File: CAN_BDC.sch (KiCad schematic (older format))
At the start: 35 parts, among them P1 CONN_01X02, P2 CONN_01X05, P3 CONN_01X02, P4 CONN_01X02, P5 CONN_01X02, P6 CONN_01X02, P7 CONN_01X04, P8 CONN_01X01, P9 CONN_01X02, U1 PSD2CAN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

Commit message: Footprint update.
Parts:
- L2: footprint Resistors_SMD:R_0805 -> Capacitors_SMD:C_1206
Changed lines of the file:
@@
 F 0 "L2" H 9500 5900 50  0000 C CNN
 F 1 "1uH" H 9500 5650 50  0000 C CNN
-F 2 "Resistors_SMD:R_0805" H 9500 5750 50  0001 C CNN
+F 2 "Capacitors_SMD:C_1206" H 9500 5750 50  0001 C CNN
 F 3 "" H 9500 5750 50  0000 C CNN
 	1    9500 5750

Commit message: Root full
Root full
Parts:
- L1: footprint usb_ccb_custom:DE0704_Coil -> usb_ccb_custom:DE0704_Coil_2
- P2: footprint usb_ccb_custom:swd_smd_conn5 -> usb_ccb_custom:swd_smd_conn5_x2
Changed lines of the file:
@@
 F 0 "P2" H 1319 1461 50  0000 C CNN
 F 1 "CONN_01X05" H 1319 1460 50  0001 C CNN
-F 2 "usb_ccb_custom:swd_smd_conn5" H 1319 1461 50  0001 C CNN
+F 2 "usb_ccb_custom:swd_smd_conn5_x2" H 1319 1461 50  0001 C CNN
 F 3 "" H 1400 1800 50  0000 C CNN
 	1    1400 1800
@@
 	-1   0    0    1
 $EndComp
+Text GLabel 3450 1500 0    60   Input ~ 0
+DRV_nENABLE
+Text GLabel 3450 1400 0    60   Input ~ 0
+DRV_MS1
+Text GLabel 5100 1400 2    60   Input ~ 0
+DRV_MS2
+Text GLabel 5100 1500 2    60   Input ~ 0
+DRV_MS3
+Text GLabel 5100 1600 2    60   Input ~ 0
+DRV_nRESET
+Text GLabel 5100 1700 2    60   Input ~ 0
+DRV_nSLEEP
+Text GLabel 5100 1800 2    60   Input ~ 0
+DRV_STEP
 Text GLabel 5100 1900 2    60   Input ~ 0
-DRV_nENABLE
-Text GLabel 5100 1800 2    60   Input ~ 0
-DRV_MS1
-Text GLabel 5100 1700 2    60   Input ~ 0
-DRV_MS2
-Text GLabel 5100 1600 2    60   Input ~ 0
-DRV_MS3
-Text GLabel 5100 1500 2    60   Input ~ 0
-DRV_nRESET
-Text GLabel 5100 1400 2    60   Input ~ 0
-DRV_nSLEEP
-Text GLabel 3450 1400 0    60   Input ~ 0
-DRV_STEP
-Text GLabel 3450 1500 0    60   Input ~ 0
 DRV_DIR
 $Comp
@@
 F 0 "L1" V 7000 5000 50  0000 L CNN
 F 1 "220uH" V 6850 4850 50  0000 L CNN
-F 2 "usb_ccb_custom:DE0704_Coil" H 6900 5050 50  0001 C CNN
+F 2 "usb_ccb_custom:DE0704_Coil_2" H 6900 5050 50  0001 C CNN
 F 3 "" H 6900 5050 50  0000 C CNN
 	1    6900 5050

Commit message: Gerber generation
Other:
- note added: "consider TCAN332DR"
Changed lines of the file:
@@
 Wire Notes Line
 	1800 3250 1800 2200
+Text Notes 2800 5750 0    60   ~ 0
+consider  TCAN332DR
 $EndSCHEMATC

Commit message: Buck-converter update.
Buck-converter update.
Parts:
- removed C5: 470p, Capacitors_SMD:C_0805, symbol CP1
- removed C6: 330u, Capacitors_SMD:c_elec_6.3x7.7, symbol CP1
- removed D1: 1N5819, Resistors_SMD:R_1206, symbol D_Schottky
- removed L1: 220uH, usb_ccb_custom:DE0704_Coil_2, symbol L_Small
- removed P8: CONN_01X01, usb_ccb_custom:smd1Conn, symbol CONN_01X01
- removed R1: 2,2k, Resistors_SMD:R_0603, symbol R
- removed R2: 0.33, Resistors_SMD:R_0603, symbol R
- removed R3: 3,9k, Resistors_SMD:R_0603, symbol R
- removed R6: 0, Resistors_SMD:R_0603, symbol R
- removed U5: MC33063, usb_ccb_custom:SOIC-8, symbol MC33063
- added U5: Mini-360, usb_ccb_custom:Mini-360, symbol Mini-360
- P2: footprint usb_ccb_custom:swd_smd_conn5_x2 -> usb_ccb_custom:swd_smd_conn5
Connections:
- wire segments 70 -> 48
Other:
- note added: "NRST\nGND\nSWCLK\nSWDIO\nVTRG"
- note removed: "GND\nSWDIO\nSWCLK\nNRST\nVTRG"
- moved on the sheet: C4, C7, L2, P6

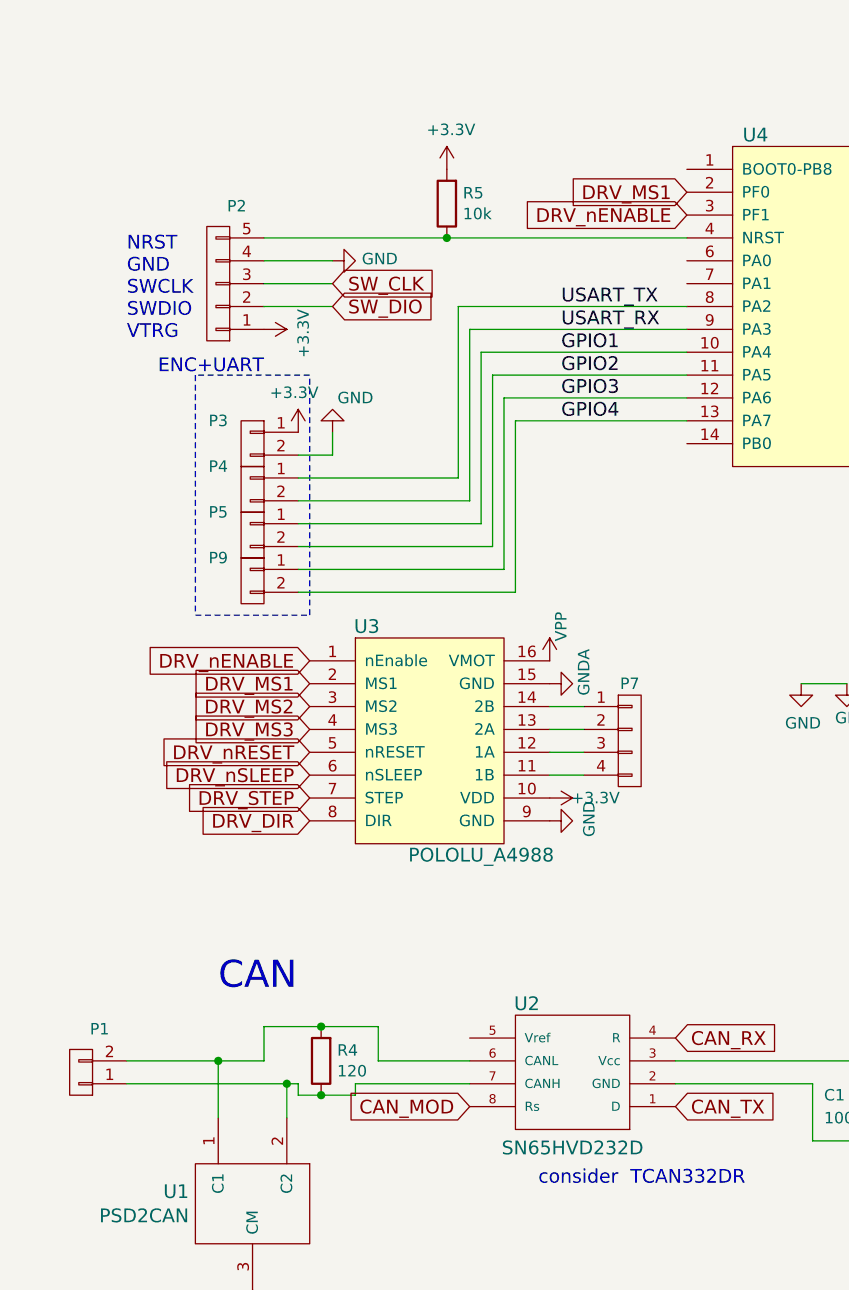
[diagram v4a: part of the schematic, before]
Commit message: Connector Footprint update
Connector Footprint update
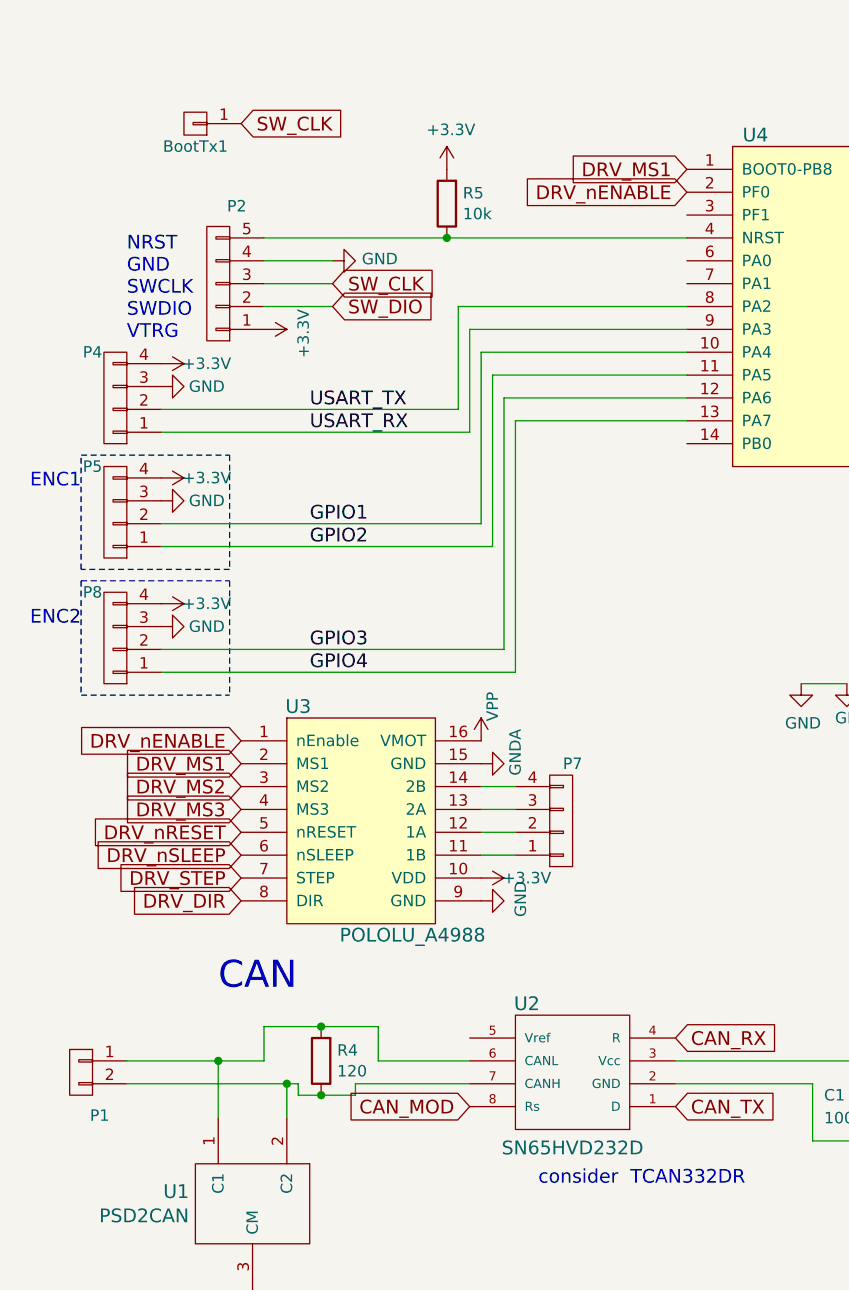
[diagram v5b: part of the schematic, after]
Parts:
- removed P3, P4, P5, P9: CONN_01X02, Pin_Headers:Pin_Header_Straight_1x02_Pitch2.00mm, symbol CONN_01X02
- added BootTx1: CONN_01X01, usb_ccb_custom:1pin, symbol CONN_01X01
- added P4, P5, P8: CONN_01X04, Pin_Headers:Pin_Header_Angled_1x04_Pitch2.54mm, symbol CONN_01X04
- C4: footprint Capacitors_SMD:c_elec_6.3x7.7 -> Capacitors_SMD:c_elec_6.3x5.3
- P1: footprint Pin_Headers:Pin_Header_Straight_1x02_Pitch2.00mm -> Pin_Headers:Pin_Header_Angled_1x02_Pitch2.54mm
- P6: footprint Pin_Headers:Pin_Header_Straight_1x02_Pitch2.00mm -> Terminal_Blocks:TerminalBlock_Pheonix_MPT-2.54mm_2pol
- P7: footprint Pin_Headers:Pin_Header_Straight_1x04 -> Terminal_Blocks:TerminalBlock_Pheonix_MPT-2.54mm_4pol
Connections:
- net +3V3: now also P4.4 (P4), P5.4 (P4), P8.4 (P4)
- net DRV_MS1: now also U4.1 (BOOT0-PB8); no longer U4.2 (PF0)
- net DRV_nENABLE: now also U4.2 (PF0); no longer U4.3 (PF1)
- net GND: now also P4.3 (P3), P5.3 (P3), P8.3 (P3)
- net GPIO1: now also P5.2 (P2)
- net GPIO2: now also P5.1 (P1)
- net GPIO3: now also P8.2 (P2)
- net GPIO4: now also P8.1 (P1)
- net SW_CLK: now also BootTx1.1 (P1)
- net USART_RX: now also P4.1 (P1)
- net USART_TX: now also P4.2 (P2)
- net at R4.2, U1.1 (C1), U2.6 (CANL): now also P1.1 (P1); no longer P1.2 (P2)
- net at R4.1, U1.2 (C2), U2.7 (CANH): now also P1.2 (P2); no longer P1.1 (P1)
- net at P7.1 (P1): now also U3.11 (1B); no longer U3.14 (2B)
- net at P7.2 (P2): now also U3.12 (1A); no longer U3.13 (2A)
- net at P7.3 (P3): now also U3.13 (2A); no longer U3.12 (1A)
- net at P7.4 (P4): now also U3.14 (2B); no longer U3.11 (1B)
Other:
- note added: "ENC1"
- note added: "ENC2"
- note removed: "ENC+UART"
- moved on the sheet: P7, U3

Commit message: Layout update
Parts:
- removed BootTx1: CONN_01X01, usb_ccb_custom:1pin, symbol CONN_01X01
- added P3, P9: CONN_01X02, Pin_Headers:Pin_Header_Straight_1x02_Pitch2.54mm, symbol CONN_01X02
- P1: footprint Pin_Headers:Pin_Header_Angled_1x02_Pitch2.54mm -> Pin_Headers:Pin_Header_Straight_1x02_Pitch2.54mm
- P4, P5, P8: footprint Pin_Headers:Pin_Header_Angled_1x04_Pitch2.54mm -> Pin_Headers:Pin_Header_Straight_1x04_Pitch2.54mm
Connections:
- net DRV_DIR: now also P3.1 (P1)
- net DRV_MS1: now also U4.2 (PF0); no longer U4.1 (BOOT0-PB8)
- net DRV_nENABLE: now also U4.3 (PF1); no longer U4.2 (PF0)
- net GND: now also P6.1 (P1); no longer P6.2 (P2)
- net SW_CLK: now also P3.2 (P2)
- net VPP: now also P6.2 (P2); no longer P6.1 (P1)
- net at P1.1 (P1), R4.2, U1.1 (C1)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: now also P9.1 (P1)
- net at P1.2 (P2), R4.1, U1.2 (C2)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: now also P9.2 (P2)

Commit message: layout update
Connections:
- net GPIO1: now also P8.1 (P1), U4.6 (PA0); no longer P5.2 (P2), U4.10 (PA4)
- net GPIO2: now also P8.2 (P2), U4.7 (PA1); no longer P5.1 (P1), U4.11 (PA5)
- net GPIO3: now also P5.1 (P1); no longer P8.2 (P2)
- net GPIO4: now also P5.2 (P2); no longer P8.1 (P1)
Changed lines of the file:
@@
 $EndDescr
 $Comp
-L GND #PWR18
+L GND #PWR01
 U 1 1 570561B2
 P 4250 2800
-F 0 "#PWR18" H 4250 2550 50  0001 C CNN
+F 0 "#PWR01" H 4250 2550 50  0001 C CNN
 F 1 "GND" H 4258 2627 50  0000 C CNN
 F 2 "" H 4250 2800 50  0000 C CNN
@@
 NRST\nGND\nSWCLK\nSWDIO\nVTRG
 $Comp
-L +3.3V #PWR10
+L +3.3V #PWR02
 U 1 1 5706E500
 P 2400 1300
-F 0 "#PWR10" H 2400 1150 50  0001 C CNN
+F 0 "#PWR02" H 2400 1150 50  0001 C CNN
 F 1 "+3.3V" H 2418 1473 50  0000 C CNN
 F 2 "" H 2400 1300 50  0000 C CNN
@@
 $EndComp
 $Comp
-L +3.3V #PWR17
+L +3.3V #PWR03
 U 1 1 5706E57B
 P 4250 1000
-F 0 "#PWR17" H 4250 850 50  0001 C CNN
+F 0 "#PWR03" H 4250 850 50  0001 C CNN
 F 1 "+3.3V" H 4268 1173 50  0000 C CNN
 F 2 "" H 4250 1000 50  0000 C CNN
@@
 $EndComp
 $Comp
-L GND #PWR22
+L GND #PWR04
 U 1 1 5706EDB2
 P 5200 3100
-F 0 "#PWR22" H 5200 2850 50  0001 C CNN
+F 0 "#PWR04" H 5200 2850 50  0001 C CNN
 F 1 "GND" H 5208 2927 50  0000 C CNN
 F 2 "" H 5200 3100 50  0000 C CNN
@@
 $EndComp
 $Comp
-L GND #PWR24
+L GND #PWR05
 U 1 1 5706EDDA
 P 5600 3100
-F 0 "#PWR24" H 5600 2850 50  0001 C CNN
+F 0 "#PWR05" H 5600 2850 50  0001 C CNN
 F 1 "GND" H 5608 2927 50  0000 C CNN
 F 2 "" H 5600 3100 50  0000 C CNN
@@
 $EndComp
 $Comp
-L +3.3V #PWR23
+L +3.3V #PWR06
 U 1 1 5706EE52
 P 5600 2800
-F 0 "#PWR23" H 5600 2650 50  0001 C CNN
+F 0 "#PWR06" H 5600 2650 50  0001 C CNN
 F 1 "+3.3V" H 5618 2973 50  0000 C CNN
 F 2 "" H 5600 2800 50  0000 C CNN
@@
 $EndComp
 $Comp
-L +3.3V #PWR21
+L +3.3V #PWR07
 U 1 1 5706EEDE
 P 5200 2800
-F 0 "#PWR21" H 5200 2650 50  0001 C CNN
+F 0 "#PWR07" H 5200 2650 50  0001 C CNN
 F 1 "+3.3V" H 5218 2973 50  0000 C CNN
 F 2 "" H 5200 2800 50  0000 C CNN
@@
 $EndComp
 $Comp
-L +3.3V #PWR20
+L +3.3V #PWR08
 U 1 1 5708A6C5
 P 4550 5200
-F 0 "#PWR20" H 4550 5050 50  0001 C CNN
+F 0 "#PWR08" H 4550 5050 50  0001 C CNN
 F 1 "+3.3V" H 4568 5373 50  0000 C CNN
 F 2 "" H 4550 5200 50  0000 C CNN
@@
 $EndComp
 $Comp
-L GND #PWR19
+L GND #PWR09
 U 1 1 5708A9FB
 P 4250 5550
-F 0 "#PWR19" H 4250 5300 50  0001 C CNN
+F 0 "#PWR09" H 4250 5300 50  0001 C CNN
 F 1 "GND" V 4258 5422 50  0000 R CNN
 F 2 "" H 4250 5550 50  0000 C CNN
@@
 $EndComp
 $Comp
-L GND #PWR7
+L GND #PWR010
 U 1 1 5708D67B
 P 1550 6200
-F 0 "#PWR7" H 1550 5950 50  0001 C CNN
+F 0 "#PWR010" H 1550 5950 50  0001 C CNN
 F 1 "GND" V 1558 6072 50  0000 R CNN
 F 2 "" H 1550 6200 50  0000 C CNN
@@
 SW_DIO
 $Comp
-L +3.3V #PWR8
+L +3.3V #PWR011
 U 1 1 57800AA2
 P 1600 2000
-F 0 "#PWR8" H 1600 1850 50  0001 C CNN
+F 0 "#PWR011" H 1600 1850 50  0001 C CNN
 F 1 "+3.3V" H 1618 2173 50  0000 C CNN
 F 2 "" H 1600 2000 50  0000 C CNN
@@
 $EndComp
 $Comp
-L +3.3V #PWR32
+L +3.3V #PWR012
 U 1 1 57F96BE3
 P 9000 2100
-F 0 "#PWR32" H 9000 1950 50  0001 C CNN
+F 0 "#PWR012" H 9000 1950 50  0001 C CNN
 F 1 "+3.3V" H 9100 2250 50  0000 C CNN
 F 2 "" H 9000 2100 50  0000 C CNN
@@
 $EndComp
 $Comp
-L GND #PWR9
+L GND #PWR013
 U 1 1 57056C83
 P 1900 1700
-F 0 "#PWR9" H 1900 1450 50  0001 C CNN
+F 0 "#PWR013" H 1900 1450 50  0001 C CNN
 F 1 "GND" V 1908 1572 50  0000 R CNN
 F 2 "" H 1900 1700 50  0000 C CNN
@@
 $EndComp
 $Comp
-L VPP #PWR29
+L VPP #PWR014
 U 1 1 5802A676
 P 7850 1550
-F 0 "#PWR29" H 7850 1400 50  0001 C CNN
+F 0 "#PWR014" H 7850 1400 50  0001 C CNN
 F 1 "VPP" H 7868 1723 50  0000 C CNN
 F 2 "" H 7850 1550 50  0000 C CNN
@@
 ENC1
 $Comp
-L GNDA #PWR30
+L GNDA #PWR015
 U 1 1 5805AC7E
 P 7850 1650
-F 0 "#PWR30" H 7850 1400 50  0001 C CNN
+F 0 "#PWR015" H 7850 1400 50  0001 C CNN
 F 1 "GNDA" H 7950 1500 50  0000 C CNN
 F 2 "" H 7850 1650 50  0000 C CNN
@@
 $EndComp
 $Comp
-L VPP #PWR11
+L VPP #PWR016
 U 1 1 5808D6A9
 P 2550 3800
-F 0 "#PWR11" H 2550 3650 50  0001 C CNN
+F 0 "#PWR016" H 2550 3650 50  0001 C CNN
 F 1 "VPP" V 2600 3950 50  0000 C CNN
 F 2 "" H 2550 3800 50  0000 C CNN
@@
 $EndComp
 $Comp
-L GNDA #PWR12
+L GNDA #PWR017
 U 1 1 5808DF8A
 P 2550 3900
-F 0 "#PWR12" H 2550 3650 50  0001 C CNN
+F 0 "#PWR017" H 2550 3650 50  0001 C CNN
 F 1 "GNDA" H 2600 3750 50  0000 C CNN
 F 2 "" H 2550 3900 50  0000 C CNN
@@
 DRV_MS3
 $Comp
-L +3.3V #PWR13
+L +3.3V #PWR018
 U 1 1 5809060D
 P 2550 4400
-F 0 "#PWR13" H 2550 4250 50  0001 C CNN
+F 0 "#PWR018" H 2550 4250 50  0001 C CNN
 F 1 "+3.3V" V 2550 4600 50  0000 C CNN
 F 2 "" H 2550 4400 50  0000 C CNN
@@
 $EndComp
 $Comp
-L GNDA #PWR26
+L GNDA #PWR019
 U 1 1 58095023
 P 7050 2350
-F 0 "#PWR26" H 7050 2100 50  0001 C CNN
+F 0 "#PWR019" H 7050 2100 50  0001 C CNN
 F 1 "GNDA" H 7150 2200 50  0000 C CNN
 F 2 "" H 7050 2350 50  0000 C CNN
@@
 $EndComp
 $Comp
-L VPP #PWR25
+L VPP #PWR020
 U 1 1 5809511F
 P 7050 2050
-F 0 "#PWR25" H 7050 1900 50  0001 C CNN
+F 0 "#PWR020" H 7050 1900 50  0001 C CNN
 F 1 "VPP" V 7100 2200 50  0000 C CNN
 F 2 "" H 7050 2050 50  0000 C CNN
@@
 $EndComp
 $Comp
-L GND #PWR33
+L GND #PWR021
 U 1 1 580A4A8C
 P 9000 2400
-F 0 "#PWR33" H 9000 2150 50  0001 C CNN
+F 0 "#PWR021" H 9000 2150 50  0001 C CNN
 F 1 "GND" H 9008 2227 50  0000 C CNN
 F 2 "" H 9000 2400 50  0000 C CNN
@@
 $EndComp
 $Comp
-L GND #PWR14
+L GND #PWR022
 U 1 1 580A6796
 P 2550 4500
-F 0 "#PWR14" H 2550 4250 50  0001 C CNN
+F 0 "#PWR022" H 2550 4250 50  0001 C CNN
 F 1 "GND" H 2558 4327 50  0000 C CNN
 F 2 "" H 2550 4500 50  0000 C CNN
@@
 $EndComp
 $Comp
-L GNDA #PWR16
+L GNDA #PWR023
 U 1 1 580A6A98
 P 4150 3550
-F 0 "#PWR16" H 4150 3300 50  0001 C CNN
+F 0 "#PWR023" H 4150 3300 50  0001 C CNN
 F 1 "GNDA" H 4200 3400 50  0000 C CNN
 F 2 "" H 4150 3550 50  0000 C CNN
@@
 $EndComp
 $Comp
-L GND #PWR15
+L GND #PWR024
 U 1 1 580A6AF4
 P 3950 3550
-F 0 "#PWR15" H 3950 3300 50  0001 C CNN
+F 0 "#PWR024" H 3950 3300 50  0001 C CNN
 F 1 "GND" H 3958 3377 50  0000 C CNN
 F 2 "" H 3950 3550 50  0000 C CNN
@@
 	1    0    0    -1
 $EndComp
-Text Label 1800 2850 0    60   ~ 0
-GPIO1
-Text Label 1800 2950 0    60   ~ 0
-GPIO2
-Text Label 1800 3400 0    60   ~ 0
-GPIO3
-Text Label 1800 3500 0    60   ~ 0
-GPIO4
 Text Notes 2800 5750 0    60   ~ 0
 consider  TCAN332DR
@@
 $EndComp
 $Comp
-L VPP #PWR27
+L VPP #PWR025
 U 1 1 586A6979
 P 7400 2100
-F 0 "#PWR27" H 7400 1950 50  0001 C CNN
+F 0 "#PWR025" H 7400 1950 50  0001 C CNN
 F 1 "VPP" V 7450 2250 50  0000 C CNN
 F 2 "" H 7400 2100 50  0000 C CNN
@@
 $EndComp
 $Comp
-L GNDA #PWR28
+L GNDA #PWR026
 U 1 1 586A6D50
 P 7400 2200
-F 0 "#PWR28" H 7400 1950 50  0001 C CNN
+F 0 "#PWR026" H 7400 1950 50  0001 C CNN
 F 1 "GNDA" H 7500 2050 50  0000 C CNN
 F 2 "" H 7400 2200 50  0000 C CNN
@@
 $EndComp
 $Comp
-L GND #PWR31
+L GND #PWR027
 U 1 1 586A7097
 P 8300 2200
-F 0 "#PWR31" H 8300 1950 50  0001 C CNN
+F 0 "#PWR027" H 8300 1950 50  0001 C CNN
 F 1 "GND" H 8308 2027 50  0000 C CNN
 F 2 "" H 8300 2200 50  0000 C CNN
@@
 $EndComp
 $Comp
-L +3.3V #PWR5
+L +3.3V #PWR028
 U 1 1 5876500B
 P 1150 3200
-F 0 "#PWR5" H 1150 3050 50  0001 C CNN
+F 0 "#PWR028" H 1150 3050 50  0001 C CNN
 F 1 "+3.3V" V 1150 3400 50  0000 C CNN
 F 2 "" H 1150 3200 50  0000 C CNN
@@
 $EndComp
 $Comp
-L GND #PWR6
+L GND #PWR029
 U 1 1 58765067
 P 1150 3300
-F 0 "#PWR6" H 1150 3050 50  0001 C CNN
+F 0 "#PWR029" H 1150 3050 50  0001 C CNN
 F 1 "GND" V 1150 3100 50  0000 C CNN
 F 2 "" H 1150 3300 50  0000 C CNN
@@
 $EndComp
 $Comp
-L +3.3V #PWR3
+L +3.3V #PWR030
 U 1 1 58765FF9
 P 1150 2650
-F 0 "#PWR3" H 1150 2500 50  0001 C CNN
+F 0 "#PWR030" H 1150 2500 50  0001 C CNN
 F 1 "+3.3V" V 1150 2850 50  0000 C CNN
 F 2 "" H 1150 2650 50  0000 C CNN
@@
 $EndComp
 $Comp
-L GND #PWR4
+L GND #PWR031
 U 1 1 5876604F
 P 1150 2750
-F 0 "#PWR4" H 1150 2500 50  0001 C CNN
+F 0 "#PWR031" H 1150 2500 50  0001 C CNN
 F 1 "GND" V 1150 2550 50  0000 C CNN
 F 2 "" H 1150 2750 50  0000 C CNN
@@
 $EndComp
 $Comp
-L +3.3V #PWR1
+L +3.3V #PWR032
 U 1 1 58766F94
 P 1150 2150
-F 0 "#PWR1" H 1150 2000 50  0001 C CNN
+F 0 "#PWR032" H 1150 2000 50  0001 C CNN
 F 1 "+3.3V" V 1150 2350 50  0000 C CNN
 F 2 "" H 1150 2150 50  0000 C CNN
@@
 $EndComp
 $Comp
-L GND #PWR2
+L GND #PWR033
 U 1 1 58766FF0
 P 1150 2250
-F 0 "#PWR2" H 1150 2000 50  0001 C CNN
+F 0 "#PWR033" H 1150 2000 50  0001 C CNN
 F 1 "GND" V 1150 2050 50  0000 C CNN
 F 2 "" H 1150 2250 50  0000 C CNN
@@
 	2450 1900 3450 1900
 Wire Wire Line
-	2600 2200 3450 2200
-Wire Wire Line
-	2650 2300 3450 2300
-Wire Wire Line
-	2700 2400 3450 2400
-Wire Wire Line
-	2550 2100 3450 2100
-Wire Wire Line
-	2650 2300 2650 3400
-Wire Wire Line
-	2700 2400 2700 3500
-Wire Wire Line
 	1600 1900 1900 1900
-Wire Wire Line
-	2600 2200 2600 2950
-Wire Wire Line
-	2600 2950 1150 2950
-Wire Wire Line
-	2550 2850 1150 2850
-Wire Wire Line
-	2550 2100 2550 2850
 Wire Notes Line
 	800  2550 1450 2550
@@
 Wire Notes Line
 	800  3100 800  3600
-Wire Wire Line
-	2650 3400 1150 3400
-Wire Wire Line
-	2700 3500 1150 3500
 Wire Notes Line
 	800  3600 1450 3600
@@
 	1200 4950 1200 5200
 Connection ~ 1200 5200
+Text GLabel 3450 2400 0    60   Input ~ 0
+GPIO4
+Text GLabel 3450 2300 0    60   Input ~ 0
+GPIO3
+Text GLabel 3450 1800 0    60   Input ~ 0
+GPIO2
+Text GLabel 3450 1700 0    60   Input ~ 0
+GPIO1
+Text GLabel 1150 3500 2    60   Input ~ 0
+GPIO1
+Text GLabel 1150 3400 2    60   Input ~ 0
+GPIO2
+Text GLabel 1150 2950 2    60   Input ~ 0
+GPIO3
+Text GLabel 1150 2850 2    60   Input ~ 0
+GPIO4
 $EndSCHEMATC
